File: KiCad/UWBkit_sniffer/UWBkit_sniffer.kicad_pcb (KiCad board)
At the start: 4 copper layers, 57.4 x 65 mm, 78 parts, among them J1 Conn_I2C1, J10 USB_C_Receptacle_USB2.0_14P, J11 USB_C_Receptacle_USB2.0_14P, J2 Conn_I2C2, J3 Conn_01x03, J4 Conn_SPIS, J5 Conn_SPIM, J6 Conn_SWD, J7 Conn_GPIO, J8 Conn_Coaxial, J9 Conn_01x02, SW1 SW_Push, T1 TestPoint_Small, T10 TestPoint_Small, T11 TestPoint_Small, T12 TestPoint_Small, T2 TestPoint_Small, T3 TestPoint_Small, T4 TestPoint_Small, T5 TestPoint_Small, T6 TestPoint_Small, T7 TestPoint_Small, T8 TestPoint_Small, T9 TestPoint_Small, U1 LBUA5QJ2AB, U2 XC9285B33CMR-G, U3 CP2104, U4 IP4234CZ6, U5 IP4234CZ6

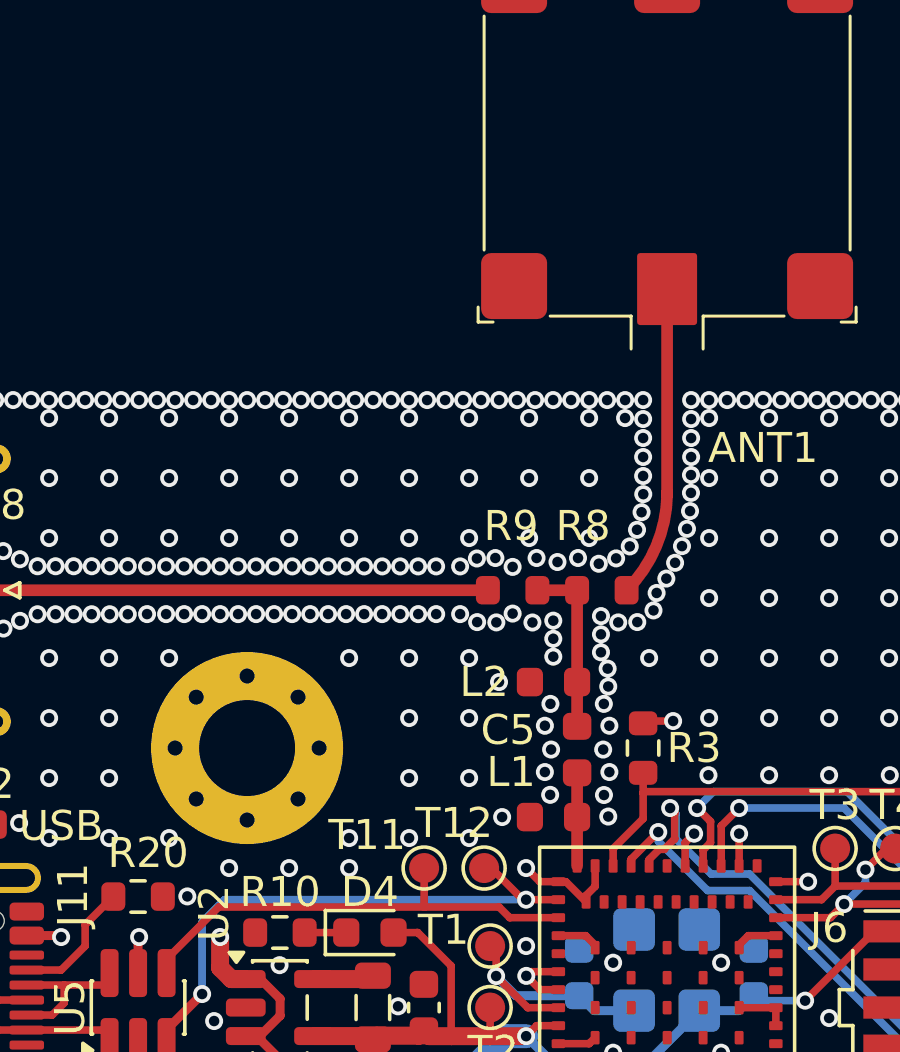
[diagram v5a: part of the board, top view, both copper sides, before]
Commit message: Moved pi-filter past R8 shorting resistor
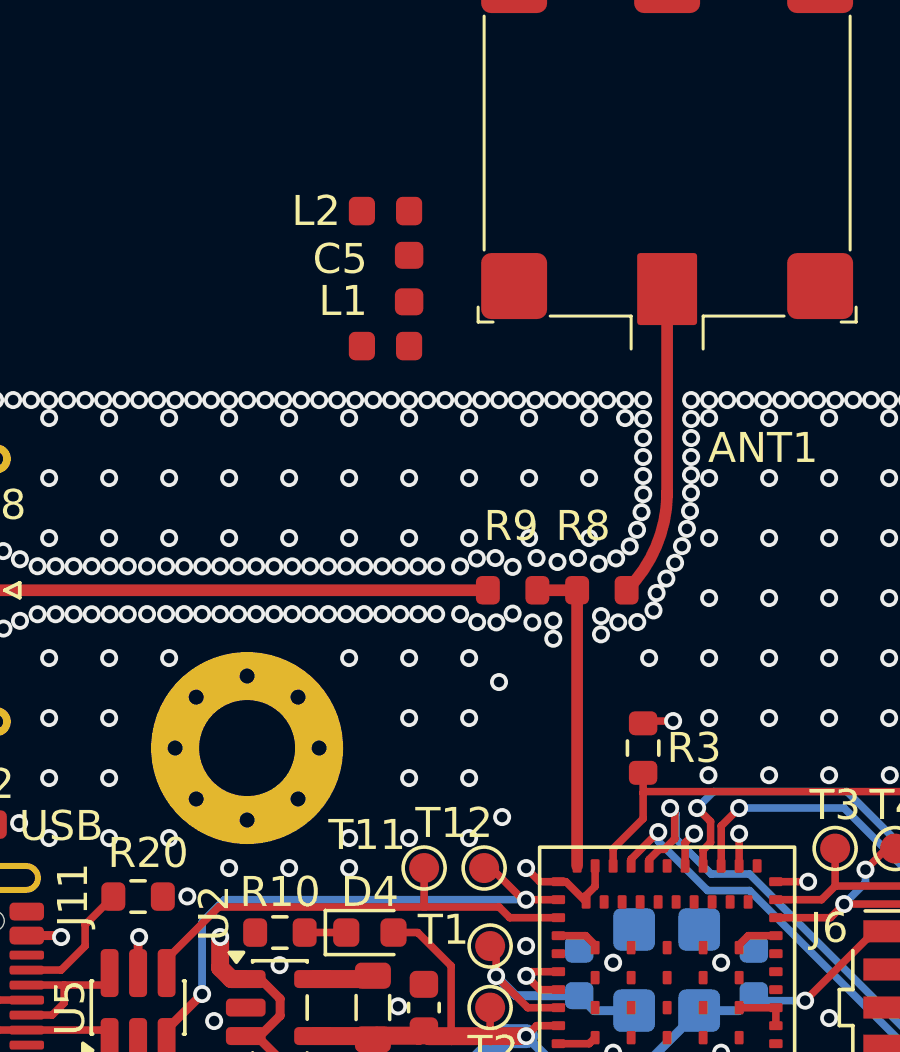
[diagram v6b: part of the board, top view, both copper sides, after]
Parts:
- moved C5 16.7 mm to (152.0, 60.4)
- moved L1 16.7 mm to (151.2, 62.6)
- moved L2 16.7 mm to (151.2, 58.1)
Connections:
- C5 pad 1: Net-(U1-ANT1) -> Net-(C5-Pad1)
- C5 pad 2: /CPU/ANT1 -> Net-(ANT1-Pad1)
- L1 pad 1: Net-(U1-ANT1) -> Net-(C5-Pad1)
- L2 pad 1: /CPU/ANT1 -> Net-(ANT1-Pad1)
- R8 pad 2: Net-(ANT1-Pad1) -> Net-(C5-Pad1)
- U1 pad 37: Net-(U1-ANT1) -> /CPU/ANT1
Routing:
- net /CPU/ANT1: track 5.86 -> 10.5 mm
- net Net-(U1-ANT1): track 3.10 -> 0.00 mm
- net GND: vias 614 -> 599

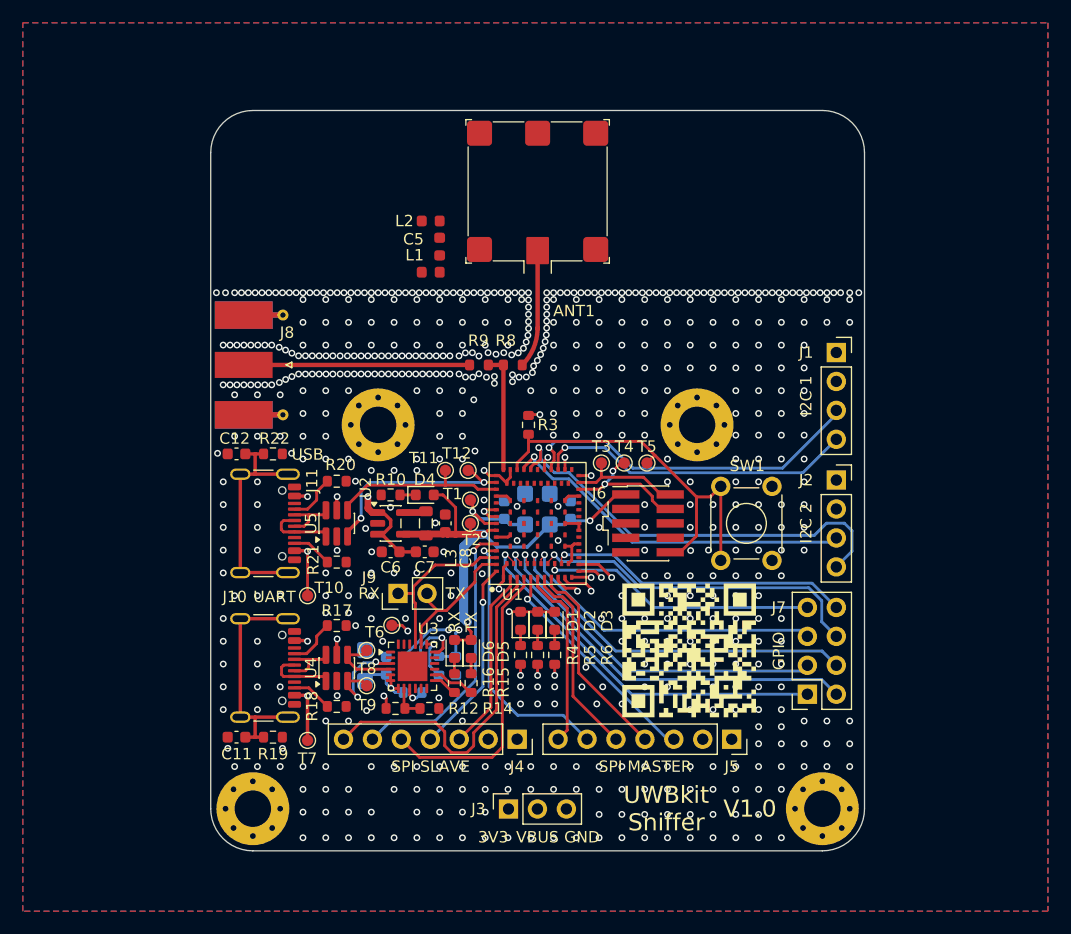
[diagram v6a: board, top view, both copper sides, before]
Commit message: Moved pi-filter
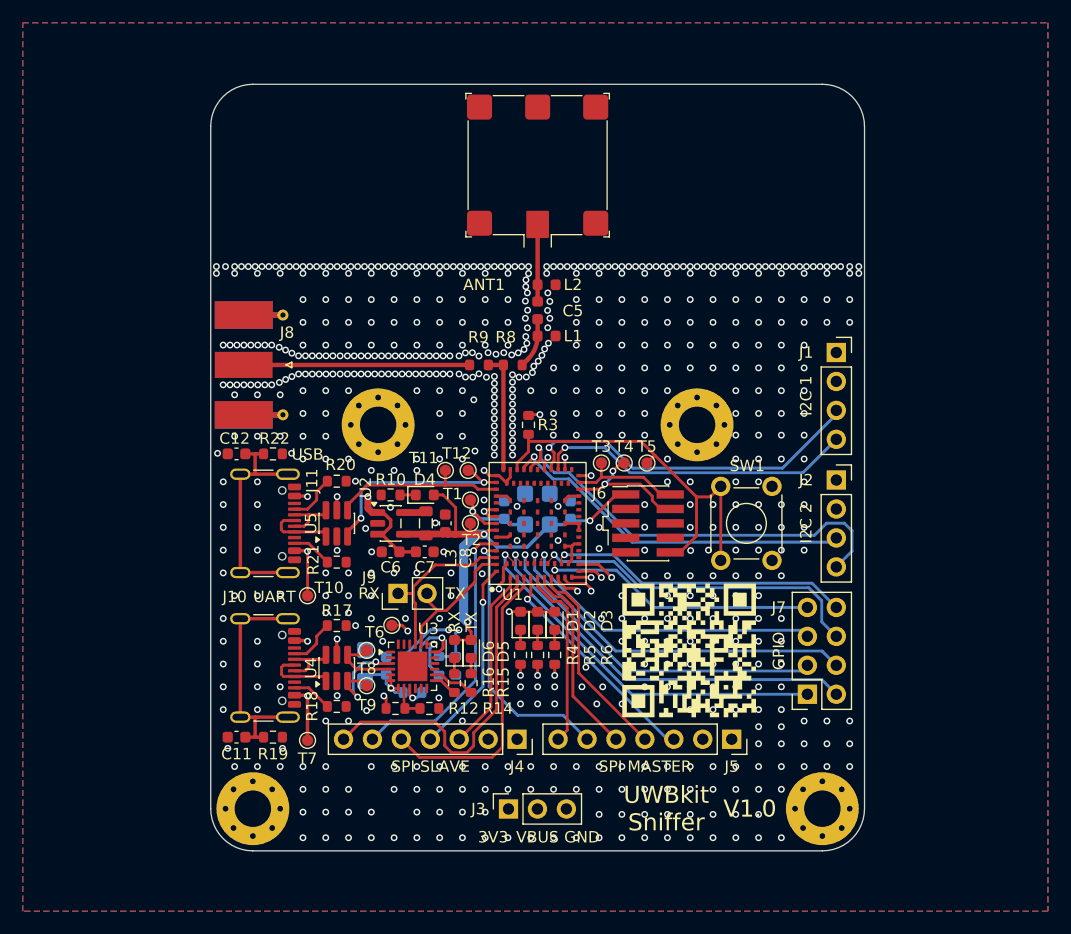
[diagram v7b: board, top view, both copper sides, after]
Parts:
- moved L1 11.6 mm to (161.4, 68.2), turned to 0 degrees
- moved L2 11.6 mm to (161.4, 63.7), turned to 0 degrees
- moved C5 10.3 mm to (160.6, 66.0)
- moved ANT1 2.30 mm to (160.6, 53.2)
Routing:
- net Net-(C5-Pad1): track 0.00 -> 4.44 mm
- net Net-(ANT1-Pad1): track 10.4 -> 6.77 mm
- net GND: vias 599 -> 646
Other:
- board size 57.4 x 65 mm -> 57.4 x 67.3 mm

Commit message: Release V1.0
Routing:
- net GND: vias 646 -> 650
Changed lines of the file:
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@@
 	)
 	(via
+		(at 163 68.8)
+		(size 0.6)
+		(drill 0.35)
+		(layers "F.Cu" "B.Cu")
+		(free yes)
+		(net 53)
+	)
+	(via
 		(at 178 62.7)
 		(size 0.6)
@@
 	)
 	(via
+		(at 163 63.1)
+		(size 0.6)
+		(drill 0.35)
+		(layers "F.Cu" "B.Cu")
+		(free yes)
+		(net 53)
+	)
+	(via
 		(at 180 83)
 		(size 0.6)
@@
 	)
 	(via
+		(at 163 67.6)
+		(size 0.6)
+		(drill 0.35)
+		(layers "F.Cu" "B.Cu")
+		(free yes)
+		(net 53)
+	)
+	(via
 		(at 143.262313 69.945)
 		(size 0.6)
@@
 	)
 	(via
+		(at 163 64.3)
+		(size 0.6)
+		(drill 0.35)
+		(layers "F.Cu" "B.Cu")
+		(free yes)
+		(net 53)
+	)
+	(via
 		(at 148 108)
 		(size 0.6)
@@
 	)
 	(zone
+		(net 79)
+		(net_name "Net-(J8-In)")
+		(layer "F.Cu")
+		(name "$teardrop_padvia$")
+		(hatch none 0.1)
+		(priority 30000)
+		(attr
+			(teardrop
+				(type padvia)
+			)
+		)
+		(connect_pads yes
+			(clearance 0)
+		)
+		(min_thickness 0.0254)
+		(filled_areas_thickness no)
+		(fill yes
+			(thermal_gap 0.5)
+			(thermal_bridge_width 0.5)
+			(island_removal_mode 1)
+			(island_area_min 10)
+		)
+		(polygon
+			(pts
+				(xy 139.34 70.935) (xy 139.34 70.545) (xy 137.34 69.595) (xy 134.799 70.74) (xy 137.34 71.885)
+			)
+		)
+	)
+	(zone
 		(net 0)
 		(net_name "")
@@
 			)
 		)
-	)
-	(zone
-		(net 79)
-		(net_name "Net-(J8-In)")
-		(layer "F.Cu")
-		(name "$teardrop_padvia$")
-		(hatch none 0.1)
-		(priority 30000)
-		(attr
-			(teardrop
-				(type padvia)
-			)
-		)
-		(connect_pads yes
-			(clearance 0)
-		)
-		(min_thickness 0.0254)
-		(filled_areas_thickness no)
-		(fill yes
-			(thermal_gap 0.5)
-			(thermal_bridge_width 0.5)
-			(island_removal_mode 1)
-			(island_area_min 10)
-		)
-		(polygon
-			(pts
-				(xy 139.34 70.935) (xy 139.34 70.545) (xy 137.34 69.595) (xy 134.799 70.74) (xy 137.34 71.885)
-			)
-		)
